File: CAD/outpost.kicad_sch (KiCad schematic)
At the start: 9 parts, among them U1 SHT41-AD1F-R2, U2 AS7343xDLG, U3 NBM5100B

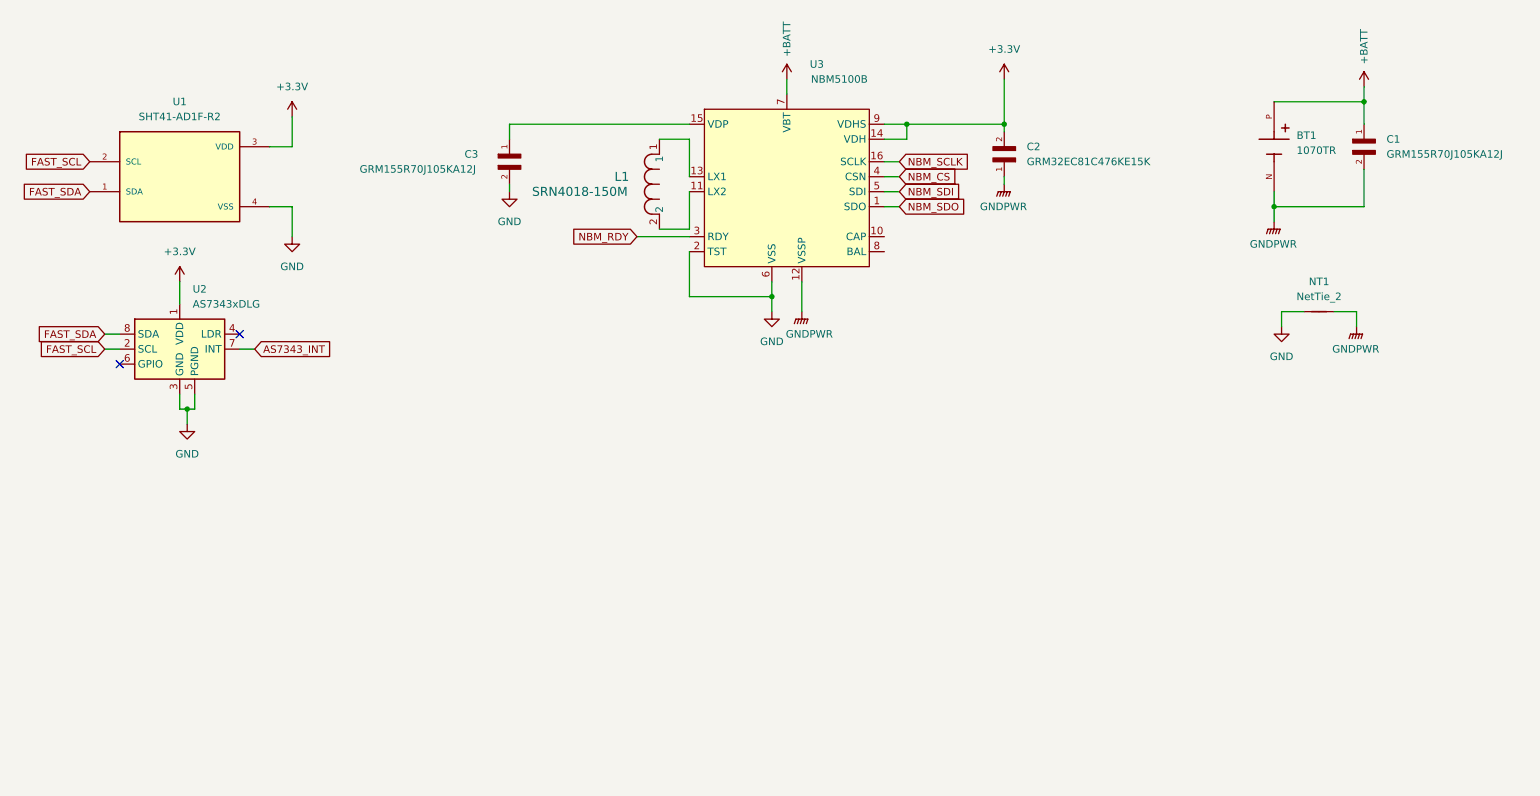
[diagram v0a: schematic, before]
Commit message: updated libraries
switched to kicad default resistors and capacitors
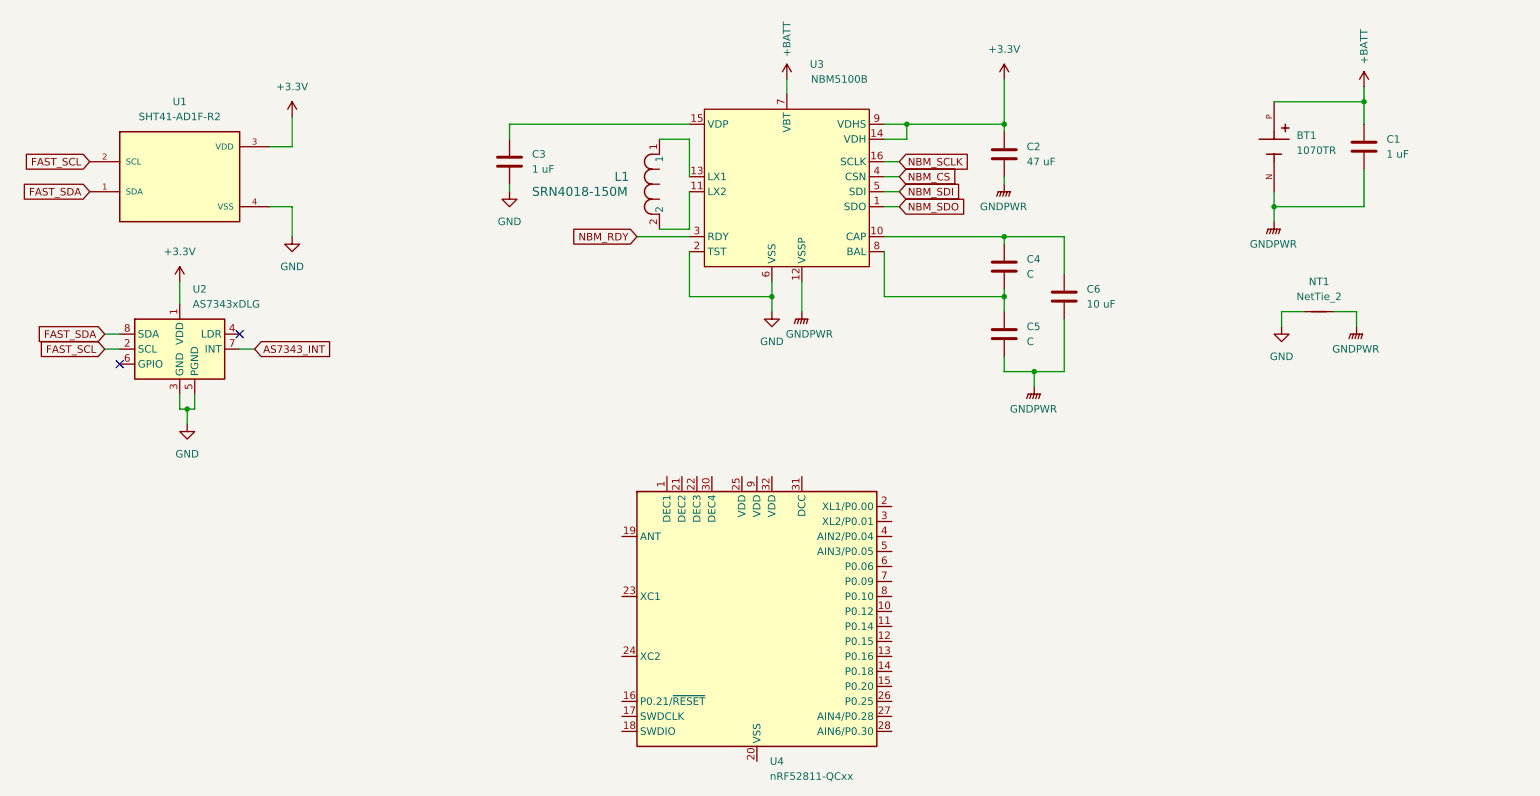
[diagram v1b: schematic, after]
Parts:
- removed C1, C3: GRM155R70J105KA12J, GRM155R70J105KA12J:CAPC1005X55N, symbol GRM155R70J105KA12J:GRM155R70J105KA12J
- removed C2: GRM32EC81C476KE15K, GRM32EC81C476KE15K:CAPC3225X270N, symbol GRM32EC81C476KE15K:GRM32EC81C476KE15K
- added C1, C3: 1 uF, Capacitor_SMD:C_0603_1608Metric_Pad1.08x0.95mm_HandSolder, symbol Device:C
- added C2: 47 uF, Capacitor_SMD:C_0603_1608Metric_Pad1.08x0.95mm_HandSolder, symbol Device:C
- added C4, C5: C, Capacitor_SMD:C_0603_1608Metric_Pad1.08x0.95mm_HandSolder, symbol Device:C
- added C6: 10 uF, Capacitor_SMD:C_0603_1608Metric_Pad1.08x0.95mm_HandSolder, symbol Device:C
- added U4: nRF52811-QCxx, Package_DFN_QFN:QFN-32-1EP_5x5mm_P0.5mm_EP3.6x3.6mm_ThermalVias, symbol MCU_Nordic:nRF52811-QCxx
- NT1: footprint (none) -> NetTie:NetTie-2_THT_Pad1.0mm
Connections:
- net +3.3V: now also C2.1
- net +BATT: now also C1.1
- net GND: now also C3.2
- net GNDPWR: now also C1.2, C2.2, C5.2, C6.2
- net at U3.10 (CAP): now also C4.1, C6.1
- net at U3.15 (VDP): now also C3.1
- net at U3.8 (BAL): now also C4.2, C5.1
- new net: U4.20 (VSS), U4.29 (VSS), U4.33 (VSS)
